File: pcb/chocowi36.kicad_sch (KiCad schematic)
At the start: 27 parts, among them SW10 SW_Push, SW11 SW_Push, SW12 SW_Push, SW14 SW_Push, SW15 SW_Push, SW16 SW_Push, SW17 SW_Push, SW18 SW_Push, SW19 SW_Push, SW2 SW_Push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

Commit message: small changes + update doc
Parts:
- H1, H2, H3, H4: footprint itsdmd:MountingHole_1.6mm_M1.4 -> itsdmd:MountingHole_2.2mm_M2
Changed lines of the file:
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@@
 			)
 		)
-		(property "Footprint" "itsdmd:MountingHole_1.6mm_M1.4"
+		(property "Footprint" "itsdmd:MountingHole_2.2mm_M2"
 			(at 139.7 120.65 0)
 			(effects
@@
 			)
 		)
-		(property "Footprint" "itsdmd:MountingHole_1.6mm_M1.4"
+		(property "Footprint" "itsdmd:MountingHole_2.2mm_M2"
 			(at 139.7 133.35 0)
 			(effects
@@
 			)
 		)
-		(property "Footprint" "itsdmd:MountingHole_1.6mm_M1.4"
+		(property "Footprint" "itsdmd:MountingHole_2.2mm_M2"
 			(at 139.7 114.3 0)
 			(effects
@@
 			)
 		)
-		(property "Footprint" "itsdmd:MountingHole_1.6mm_M1.4"
+		(property "Footprint" "itsdmd:MountingHole_2.2mm_M2"
 			(at 139.7 127 0)
 			(effects

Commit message: update routing to support placing tactile switches on both sides
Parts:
- added SW_POWER2: SW_SPDT, itsdmd:SW-S_MSK-12C02, symbol itsdmd:SK12D07VG4
- added SW_RST2: SW_Push, itsdmd:SW-T_SPST_TL3342, symbol Switch:SW_Push
- SW_RST1: footprint itsdmd:SW-T_7.4x2.6-4pad-smd -> itsdmd:SW-T_SPST_TL3342
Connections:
- net +BATT: now also SW_POWER2.2
- net gnd: now also SW_RST2.1
- net reset: now also SW_RST2.2
- net at BT1.1 (+), SW_POWER1.COM: now also SW_POWER2.COM
- no-connect marks 3 -> 4

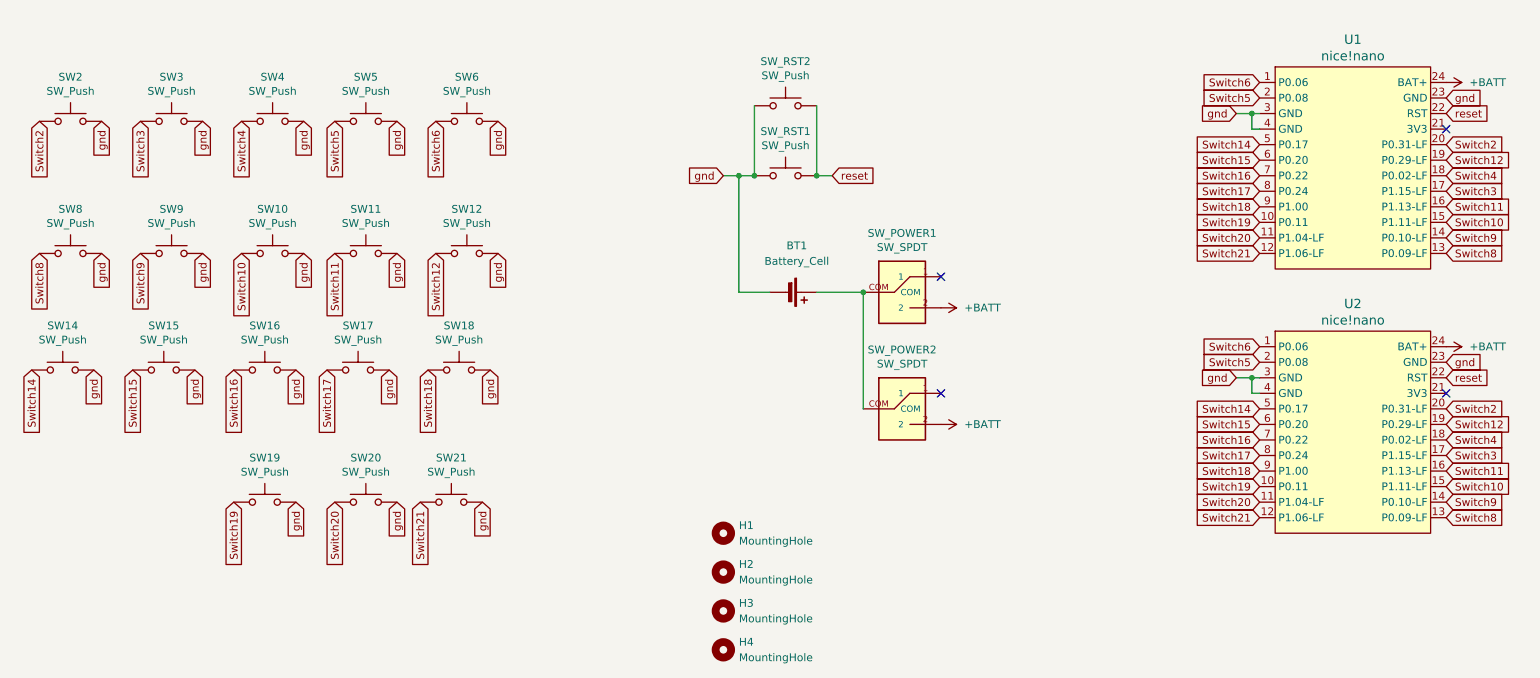
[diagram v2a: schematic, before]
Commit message: add tp4056 charging module, update edge.cut
change power button position
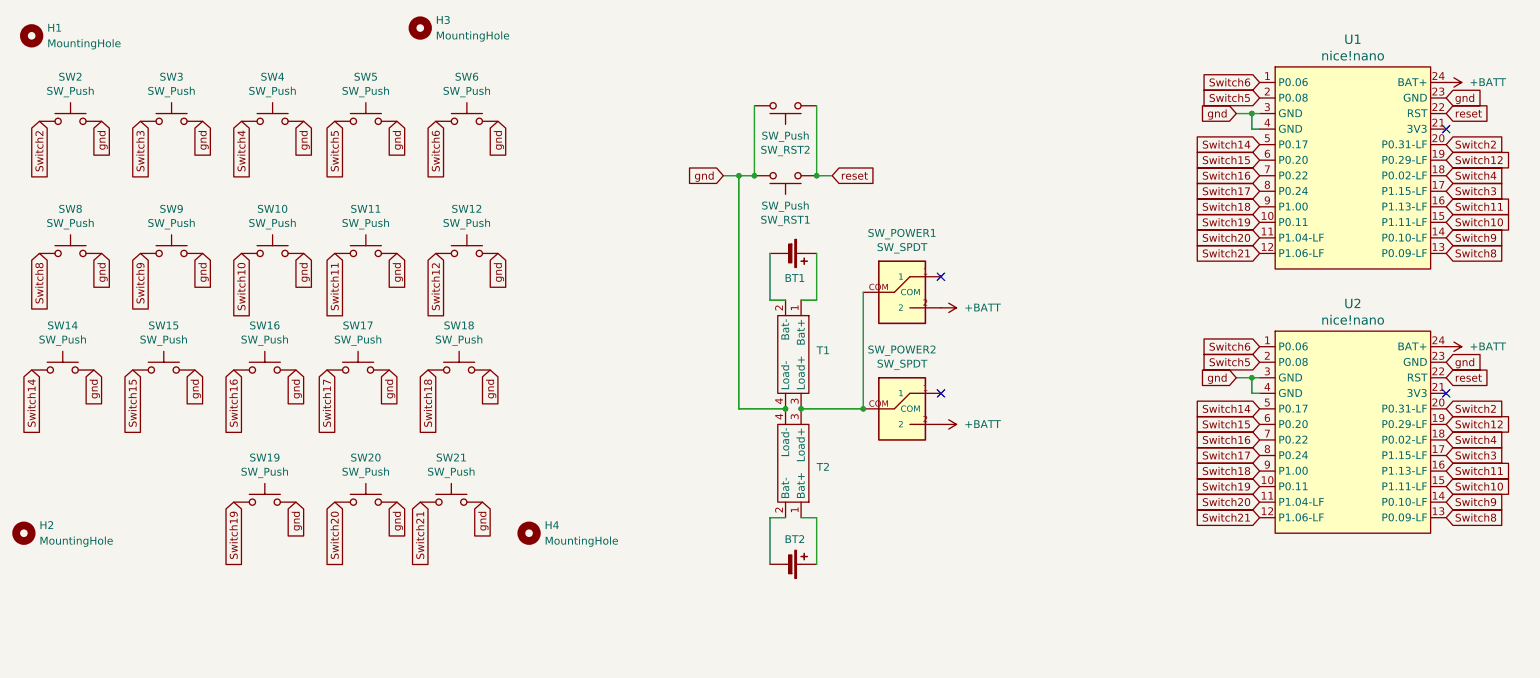
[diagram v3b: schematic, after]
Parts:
- added BT2: B1, itsdmd:Battery_Pads-dual-side, symbol Device:Battery_Cell
- added T1, T2: ~, itsdmd:Module_TP4056_Mini-SMD_Interface, symbol itsdmd:TP4056_Module_Mini
- BT1: value Battery_Cell -> B1
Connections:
- net gnd: now also T1.4 (Load-), T2.4 (Load-); no longer BT1.2 (-)
- net at SW_POWER1.COM, SW_POWER2.COM: now also T1.3 (Load+), T2.3 (Load+); no longer BT1.1 (+)
- new net: BT1.1 (+), T1.1 (Bat+)
- new net: BT1.2 (-), T1.2 (Bat-)
- new net: BT2.1 (+), T2.1 (Bat+)
- new net: BT2.2 (-), T2.2 (Bat-)
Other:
- moved on the sheet: BT1, H1, H2, H3, H4, SW_RST1, SW_RST2
